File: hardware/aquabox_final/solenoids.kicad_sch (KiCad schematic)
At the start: 0 parts

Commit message: Acionamento da bom e solenóides
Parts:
- added D10: 1N4007, Diode_THT:D_DO-41_SOD81_P10.16mm_Horizontal, symbol Diode:1N4007
- added D9: LED, symbol Device:LED
- added J8: Screw_Terminal_01x04, symbol Connector:Screw_Terminal_01x04
- added K1: Relay_SPDT, symbol Relay:Relay_SPDT
- added Q1, Q10, Q3, Q5: BC337, Package_TO_SOT_THT:TO-92_Inline, symbol Transistor_BJT:BC337
- added Q2, Q4, Q6: BC327, Package_TO_SOT_THT:TO-92_Inline, symbol Transistor_BJT:BC327
- added Q7, Q8, Q9: IRLZ44N, Package_TO_SOT_THT:TO-220-3_Vertical, symbol Transistor_FET:IRLZ44N
- added R28, R29, R30, R41: 1K, symbol Device:R
- added R31, R32, R33, R37, R38, R39: 10K, symbol Device:R
- added R34, R35, R36: 10R, symbol Device:R
- added R40, R42: 220R, symbol Device:R
- added U10, U11, U12, U13: PC817, Package_DIP:DIP-4_W7.62mm, symbol Isolator:PC817
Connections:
- new net: R30.1, U12.2
- new net: Q5.2 (B), Q6.2 (B), R33.1, U12.3
- new net: R29.1, U11.2
- new net: D10.2 (A), D9.1 (K), K1.A2, Q10.1 (C)
- new net: Q10.2 (B), R41.2
- new net: D9.2 (A), R42.2
- new net: Q5.3 (E), Q6.1 (C), R36.1
- new net: Q9.1 (G), R36.2, R39.1
- new net: R40.2, U13.1
- new net: R41.1, U13.3
- new net: Q3.2 (B), Q4.2 (B), R32.1, U11.3
- new net: Q7.1 (G), R34.2, R37.1
- new net: Q1.2 (B), Q2.2 (B), R31.1, U10.3
- new net: Q3.3 (E), Q4.1 (C), R35.1
- new net: Q1.3 (E), Q2.1 (C), R34.1
- new net: R28.1, U10.2
- new net: Q8.1 (G), R35.2, R38.1
- new net +12V: J8.1 (Pin_1), Q1.1 (C), Q3.1 (C), Q5.1 (C), U10.4, U11.4, U12.4
- new net +5V: D10.1 (K), K1.A1, R42.1, U13.4
- new net GND: Q10.3 (E), R28.2, R29.2, R30.2, U13.2
- new net GND1: Q2.3 (E), Q4.3 (E), Q6.3 (E), Q7.3 (S), Q8.3 (S), Q9.3 (S), R31.2, R32.2, R33.2, R37.2, R38.2, R39.2
- new net RELAY_PUMP: R40.1
- new net SOL_1: U10.1
- new net SOL_2: U11.1
- new net SOL_3: U12.1
- new net SOL_MOSFET_1: J8.2 (Pin_2), Q7.2 (D)
- new net SOL_MOSFET_2: J8.3 (Pin_3), Q8.2 (D)
- new net SOL_MOSFET_3: J8.4 (Pin_4), Q9.2 (D)
- no-connect marks 0 -> 1
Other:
- company: (none) -> INVENCTUS Soluções Tecnológicas
- title: (none) -> Solenóides e Bomba

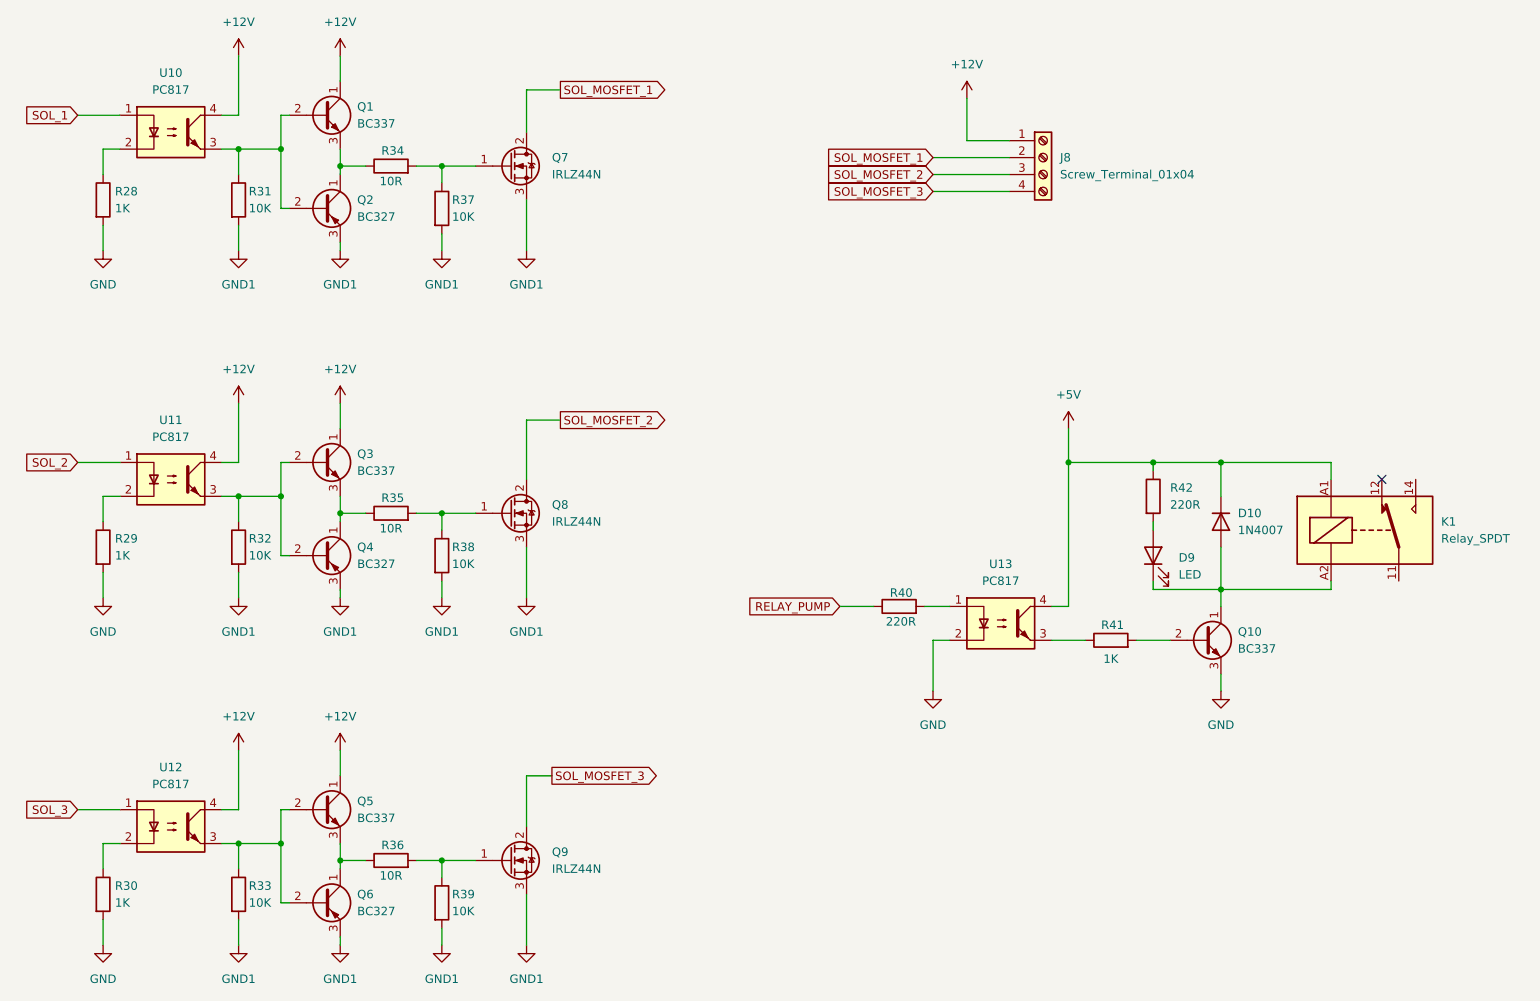
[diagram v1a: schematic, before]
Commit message: Implementação do RTC
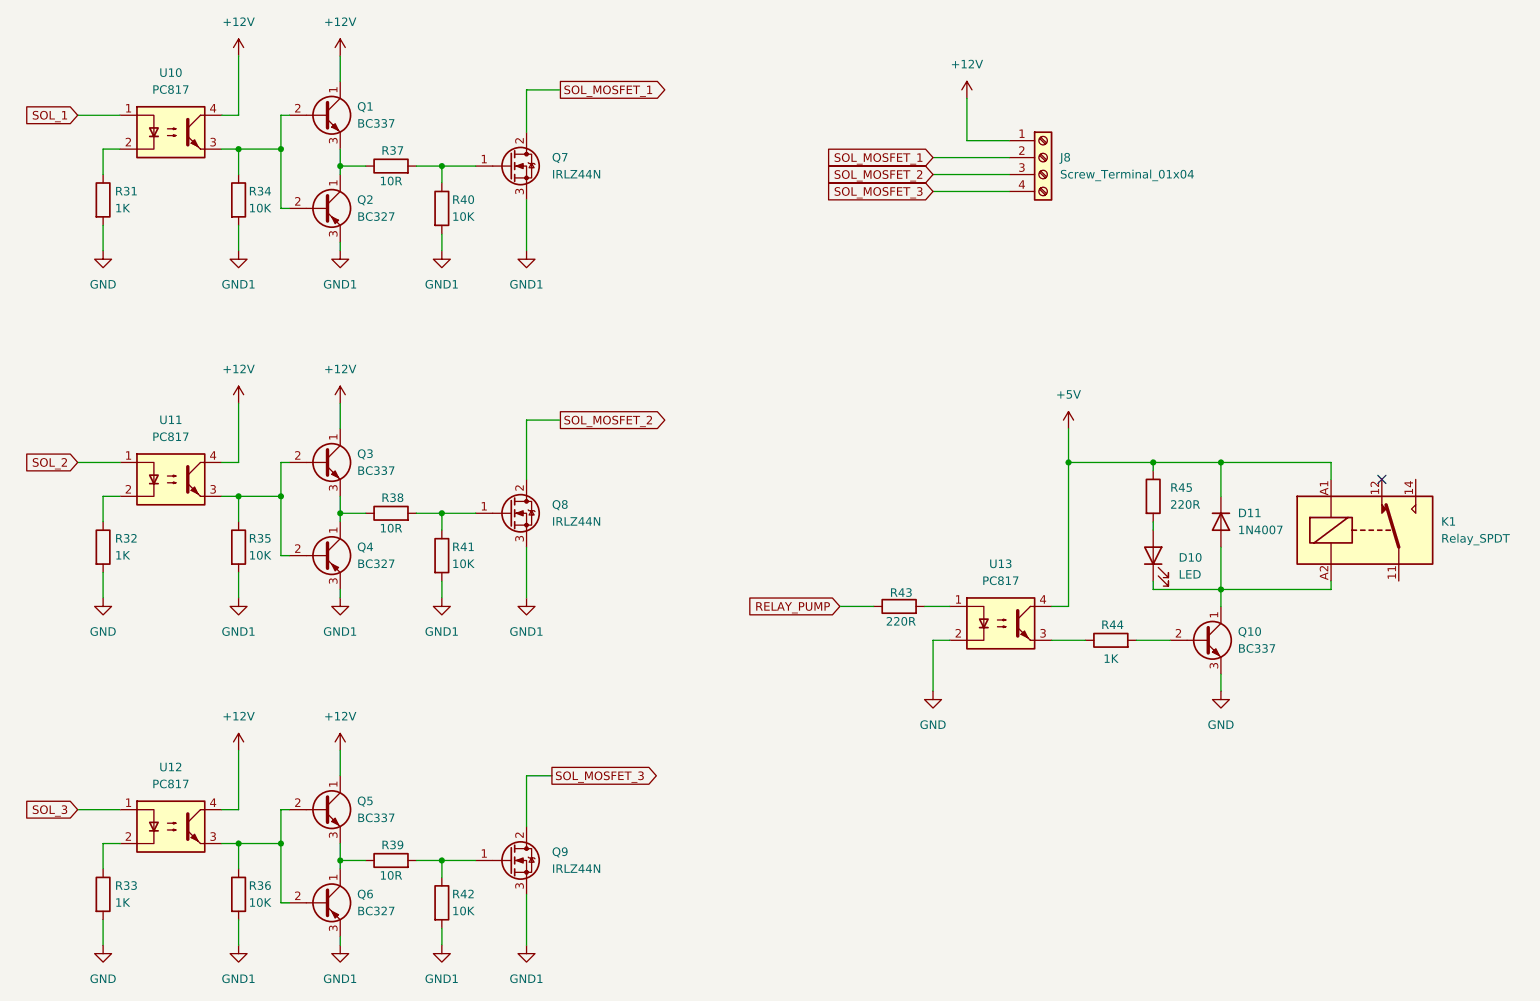
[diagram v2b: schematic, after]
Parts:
- renumbered D9 to D10, D10 to D11, R28 to R31, R29 to R32, R30 to R33, R31 to R34, R32 to R35, R33 to R36, R34 to R37, R35 to R38, R36 to R39, R37 to R40, R38 to R41, R39 to R42, R40 to R43, R41 to R44, R42 to R45

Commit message: Atualização
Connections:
- net +5V is gone; now on net +12V: D11.1 (K), K1.A1, R45.1, U13.4
- net GND: no longer Q10.3 (E)
- net GND1: now also Q10.3 (E)
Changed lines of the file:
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@@
 	)
 	(junction
-		(at 190.5 92.71)
-		(diameter 0)
-		(color 0 0 0 0)
-	)
-	(junction
 		(at 72.39 45.72)
 		(diameter 0)
@@
 	(wire
 		(pts
-			(xy 190.5 87.63) (xy 190.5 92.71)
-		)
-		(stroke
-			(width 0)
-			(type default)
-		)
-	)
-	(wire
-		(pts
 			(xy 170.18 119.38) (xy 170.18 127)
 		)
@@
 	(wire
 		(pts
+			(xy 213.36 124.46) (xy 213.36 127)
+		)
+		(stroke
+			(width 0)
+			(type default)
+		)
+	)
+	(wire
+		(pts
 			(xy 72.39 97.79) (xy 72.39 106.68)
 		)
@@
 	(wire
 		(pts
-			(xy 213.36 124.46) (xy 213.36 127)
-		)
-		(stroke
-			(width 0)
-			(type default)
-		)
-	)
-	(wire
-		(pts
 			(xy 109.22 139.7) (xy 109.22 147.32)
 		)
@@
 	(wire
 		(pts
+			(xy 213.36 87.63) (xy 213.36 92.71)
+		)
+		(stroke
+			(width 0)
+			(type default)
+		)
+	)
+	(wire
+		(pts
 			(xy 73.66 40.64) (xy 72.39 40.64)
 		)
@@
 	)
 	(symbol
-		(lib_id "power:+12V")
-		(at 66.04 31.75 0)
+		(lib_id "power:GND1")
+		(at 213.36 127 0)
 		(unit 1)
 		(body_style 1)
@@
 		(dnp no)
 		(fields_autoplaced yes)
-		(property "Reference" "#PWR046"
-			(at 66.04 35.56 0)
+		(property "Reference" "#PWR066"
+			(at 213.36 133.35 0)
 			(hide yes)
 			(show_name no)
@@
 			)
 		)
-		(property "Value" "+12V"
-			(at 66.04 26.67 0)
+		(property "Value" "GND1"
+			(at 213.36 132.08 0)
 			(show_name no)
 			(do_not_autoplace no)
@@
 		)
 		(property "Footprint" ""
-			(at 66.04 31.75 0)
+			(at 213.36 127 0)
 			(hide yes)
 			(show_name no)
@@
 		)
 		(property "Datasheet" ""
-			(at 66.04 31.75 0)
+			(at 213.36 127 0)
 			(hide yes)
 			(show_name no)
@@
 			)
 		)
-		(property "Description" "Power symbol creates a global label with name \"+12V\""
-			(at 66.04 31.75 0)
+		(property "Description" "Power symbol creates a global label with name \"GND1\" , ground"
+			(at 213.36 127 0)
 			(hide yes)
 			(show_name no)
@@
 			(project "aquabox_final"
 				(path "/c895ac8d-c639-4fea-ba83-739985d9c75e/ef4d3825-84ec-47ae-a142-b70e289b2098"
-					(reference "#PWR046")
+					(reference "#PWR066")
 					(unit 1)
 				)
@@
 	)
 	(symbol
-		(lib_id "power:GND")
-		(at 213.36 127 0)
+		(lib_id "power:+12V")
+		(at 66.04 31.75 0)
 		(unit 1)
 		(body_style 1)
@@
 		(dnp no)
 		(fields_autoplaced yes)
-		(property "Reference" "#PWR067"
-			(at 213.36 133.35 0)
+		(property "Reference" "#PWR046"
+			(at 66.04 35.56 0)
 			(hide yes)
 			(show_name no)
@@
 			)
 		)
-		(property "Value" "GND"
-			(at 213.36 132.08 0)
+		(property "Value" "+12V"
+			(at 66.04 26.67 0)
 			(show_name no)
 			(do_not_autoplace no)
@@
 		)
 		(property "Footprint" ""
-			(at 213.36 127 0)
+			(at 66.04 31.75 0)
 			(hide yes)
 			(show_name no)
@@
 		)
 		(property "Datasheet" ""
-			(at 213.36 127 0)
+			(at 66.04 31.75 0)
 			(hide yes)
 			(show_name no)
@@
 			)
 		)
-		(property "Description" "Power symbol creates a global label with name \"GND\" , ground"
-			(at 213.36 127 0)
+		(property "Description" "Power symbol creates a global label with name \"+12V\""
+			(at 66.04 31.75 0)
 			(hide yes)
 			(show_name no)
@@
 			(project "aquabox_final"
 				(path "/c895ac8d-c639-4fea-ba83-739985d9c75e/ef4d3825-84ec-47ae-a142-b70e289b2098"
-					(reference "#PWR067")
+					(reference "#PWR046")
 					(unit 1)
 				)
@@
 	)
 	(symbol
-		(lib_id "power:+5V")
-		(at 190.5 87.63 0)
-		(unit 1)
-		(body_style 1)
-		(exclude_from_sim no)
-		(in_bom yes)
-		(on_board yes)
-		(in_pos_files yes)
-		(dnp no)
-		(fields_autoplaced yes)
-		(property "Reference" "#PWR066"
-			(at 190.5 91.44 0)
-			(hide yes)
-			(show_name no)
-			(do_not_autoplace no)
-			(effects
-				(font
-					(size 1.27 1.27)
-				)
-			)
-		)
-		(property "Value" "+5V"
-			(at 190.5 82.55 0)
-			(show_name no)
-			(do_not_autoplace no)
-			(effects
-				(font
-					(size 1.27 1.27)
-				)
-			)
-		)
-		(property "Footprint" ""
-			(at 190.5 87.63 0)
-			(hide yes)
-			(show_name no)
-			(do_not_autoplace no)
-			(effects
-				(font
-					(size 1.27 1.27)
-				)
-			)
-		)
-		(property "Datasheet" ""
-			(at 190.5 87.63 0)
-			(hide yes)
-			(show_name no)
-			(do_not_autoplace no)
-			(effects
-				(font
-					(size 1.27 1.27)
-				)
-			)
-		)
-		(property "Description" "Power symbol creates a global label with name \"+5V\""
-			(at 190.5 87.63 0)
-			(hide yes)
-			(show_name no)
-			(do_not_autoplace no)
-			(effects
-				(font
-					(size 1.27 1.27)
-				)
-			)
-		)
-		(pin "1"
-		)
-		(instances
-			(project "aquabox_final"
-				(path "/c895ac8d-c639-4fea-ba83-739985d9c75e/ef4d3825-84ec-47ae-a142-b70e289b2098"
-					(reference "#PWR066")
-					(unit 1)
-				)
-			)
-		)
-	)
-	(symbol
 		(lib_id "Transistor_BJT:BC327")
 		(at 78.74 54.61 0)
@@
 					(unit 1)
 				)
+			)
+		)
+	)
+	(symbol
+		(lib_id "power:+12V")
+		(at 213.36 87.63 0)
+		(unit 1)
+		(body_style 1)
+		(exclude_from_sim no)
+		(in_bom yes)
+		(on_board yes)
+		(in_pos_files yes)
+		(dnp no)
+		(fields_autoplaced yes)
+		(property "Reference" "#PWR067"
+			(at 213.36 91.44 0)
+			(hide yes)
+			(show_name no)
+			(do_not_autoplace no)
+			(effects
+				(font
+					(size 1.27 1.27)
+				)
+			)
+		)
+		(property "Value" "+12V"
+			(at 213.36 82.55 0)
+			(show_name no)
+			(do_not_autoplace no)
+			(effects
+				(font
+					(size 1.27 1.27)
+				)
+			)
+		)
+		(property "Footprint" ""
+			(at 213.36 87.63 0)
+			(hide yes)
+			(show_name no)
+			(do_not_autoplace no)
+			(effects
+				(font
+					(size 1.27 1.27)
+				)
+			)
+		)
+		(property "Datasheet" ""
+			(at 213.36 87.63 0)
+			(hide yes)
+			(show_name no)
+			(do_not_autoplace no)
+			(effects
+				(font
+					(size 1.27 1.27)
+				)
+			)
+		)
+		(property "Description" "Power symbol creates a global label with name \"+12V\""
+			(at 213.36 87.63 0)
+			(hide yes)
+			(show_name no)
+			(do_not_autoplace no)
+			(effects
+				(font
+					(size 1.27 1.27)
+				)
+			)
+		)
+		(pin "1"
+		)
+		(instances
+			(project "aquabox_final"
+				(path "/c895ac8d-c639-4fea-ba83-739985d9c75e/ef4d3825-84ec-47ae-a142-b70e289b2098"
+					(reference "#PWR067")
+					(unit 1)
+				)
